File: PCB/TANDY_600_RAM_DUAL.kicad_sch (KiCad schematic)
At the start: 7 parts, among them CN1 TANDY_600_RAM_BUS, CN2 TANDY_600_RAM_BUS, U1 AS6C2008A, U2 74HC148, U3 74LVC1G02

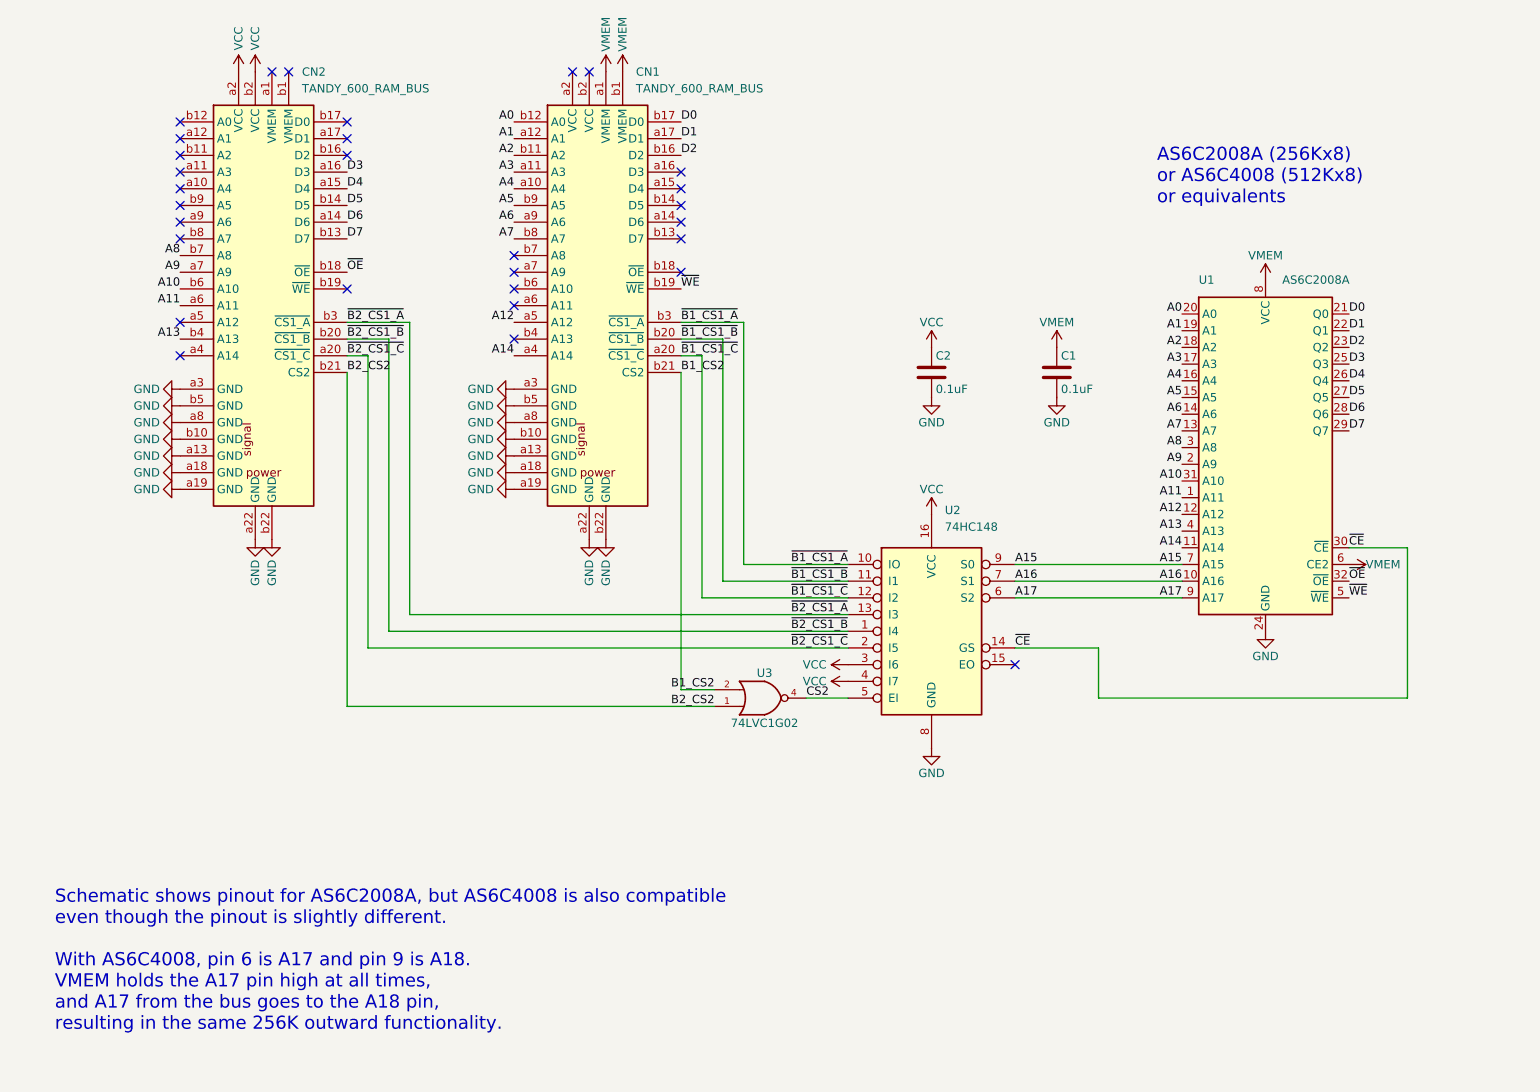
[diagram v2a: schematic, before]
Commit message: dual version add /CE pullup for battery life
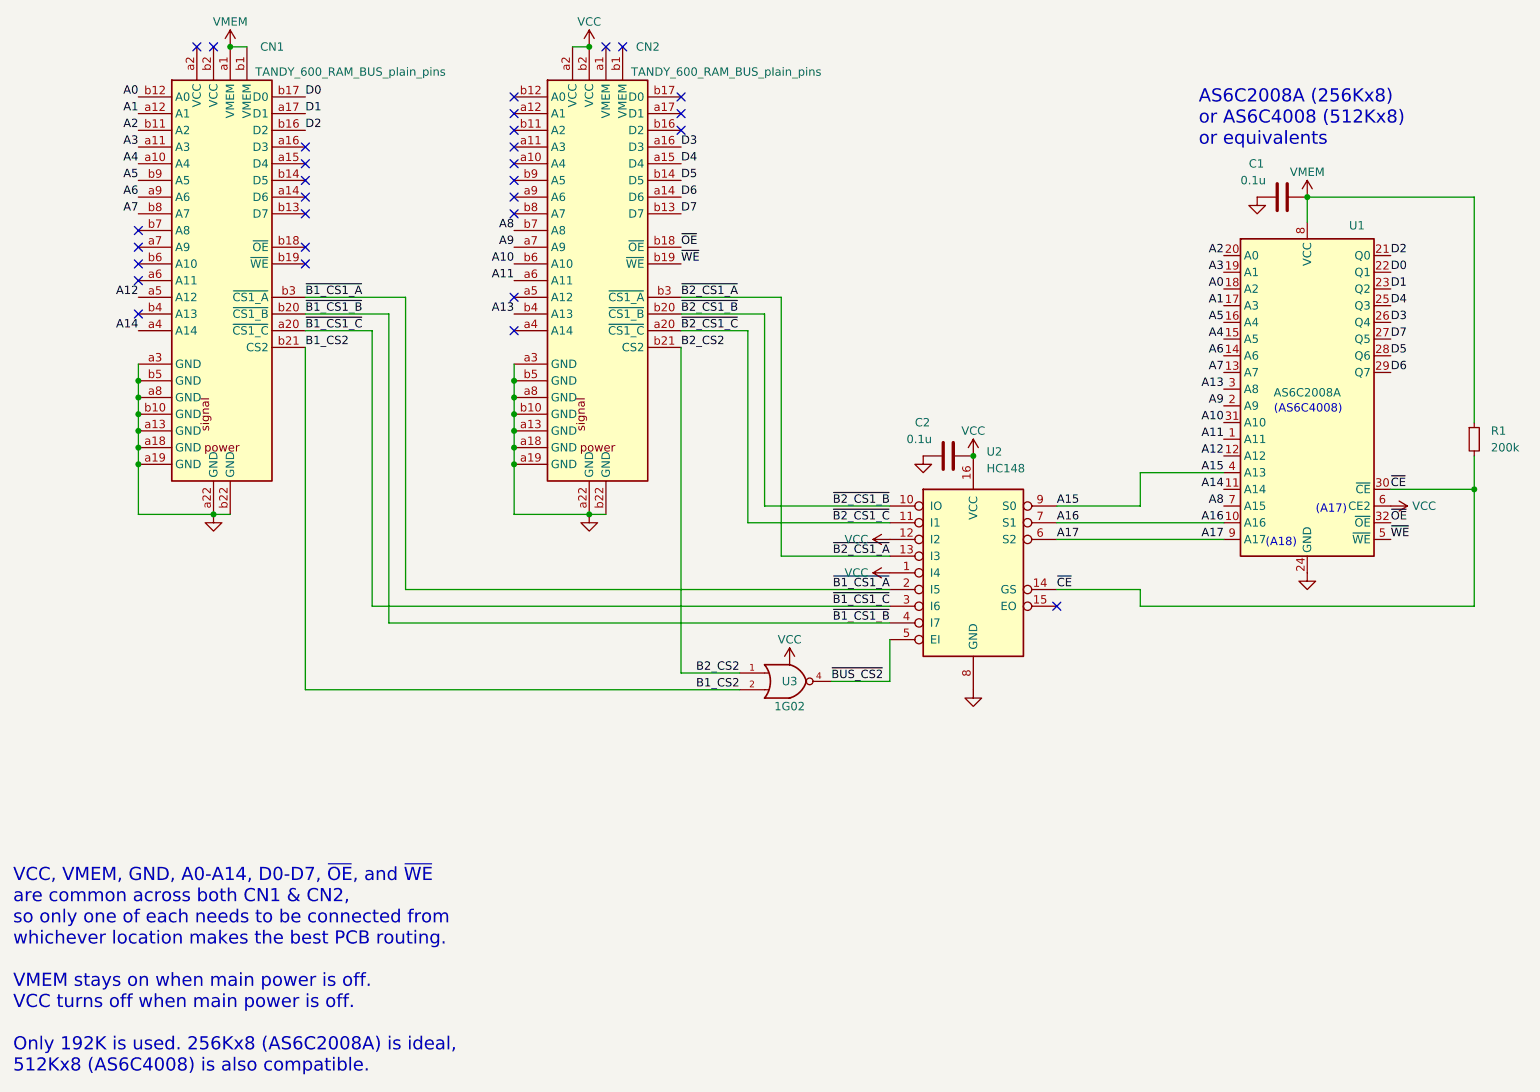
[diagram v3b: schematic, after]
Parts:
- added R1: 200k, 000_LOCAL:R_0805, symbol 000_LOCAL:R_Small
- C1, C2: value 0.1uF -> 0.1u
- CN1, CN2: value TANDY_600_RAM_BUS -> TANDY_600_RAM_BUS_plain_pins
- U2: value 74HC148 -> HC148
- U3: value 74LVC1G02 -> 1G02
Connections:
- net A0: now also U1.18 (A2); no longer U1.20 (A0)
- net A1: now also U1.17 (A3); no longer U1.19 (A1)
- net A13: now also U1.3 (A8); no longer U1.4 (A13)
- net A15: now also U1.4 (A13); no longer U1.7 (A15)
- net A2: now also U1.20 (A0); no longer U1.18 (A2)
- net A3: now also U1.19 (A1); no longer U1.17 (A3)
- net A4: now also U1.15 (A5); no longer U1.16 (A4)
- net A5: now also U1.16 (A4); no longer U1.15 (A5)
- net A8: now also U1.7 (A15); no longer U1.3 (A8)
- net D0: now also U1.22 (Q1); no longer U1.21 (Q0)
- net D1: now also U1.23 (Q2); no longer U1.22 (Q1)
- net D2: now also U1.21 (Q0); no longer U1.23 (Q2)
- net D3: now also U1.26 (Q4); no longer U1.25 (Q3)
- net D4: now also U1.25 (Q3); no longer U1.26 (Q4)
- net D5: now also U1.28 (Q6); no longer U1.27 (Q5)
- net D6: now also U1.29 (Q7); no longer U1.28 (Q6)
- net D7: now also U1.27 (Q5); no longer U1.29 (Q7)
- net VCC: now also U1.6 (CE2), U2.1 (I4), U2.12 (I2); no longer U2.3 (I6), U2.4 (I7)
- net VMEM: now also R1.1; no longer U1.6 (CE2)
- net ~{B1_CS1_A}: now also U2.2 (I5); no longer U2.10 (IO)
- net ~{B1_CS1_B}: now also U2.4 (I7); no longer U2.11 (I1)
- net ~{B1_CS1_C}: now also U2.3 (I6); no longer U2.12 (I2)
- net ~{B2_CS1_B}: now also U2.10 (IO); no longer U2.1 (I4)
- net ~{B2_CS1_C}: now also U2.11 (I1); no longer U2.2 (I5)
- net ~{CE}: now also R1.2
- net ~{WE}: now also CN2.b19 (~{WE}); no longer CN1.b19 (~{WE})
- net CS2 renamed ~{BUS_CS2}
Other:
- note added: "(A17)"
- note added: "(A18)"
- note added: "(AS6C4008)"
- note added: "VCC, VMEM, GND, A0-A14, D0-D7, ~{OE}, and ~{WE} are common across both CN1 & CN2, so only one of each needs to be connected from whichever location makes the best PCB routing. VMEM stays on when main power is off. VCC turns off when main power is off. Only 192K is used. 256Kx8 (AS6C2008A) is ideal, 512Kx8 (AS6C4008) is also compatible."
- note removed: "Schematic shows pinout for AS6C2008A, but AS6C4008 is also compatible even though the pinout is slightly different. With AS6C4008, pin 6 is A17 and pin 9 is A18. VMEM holds the A17 pin high at all times, and A17 from the bus goes to the A18 pin, resulting in the same 256K outward functionality."
- moved on the sheet: C1, C2, CN1, CN2, U1, U2, U3

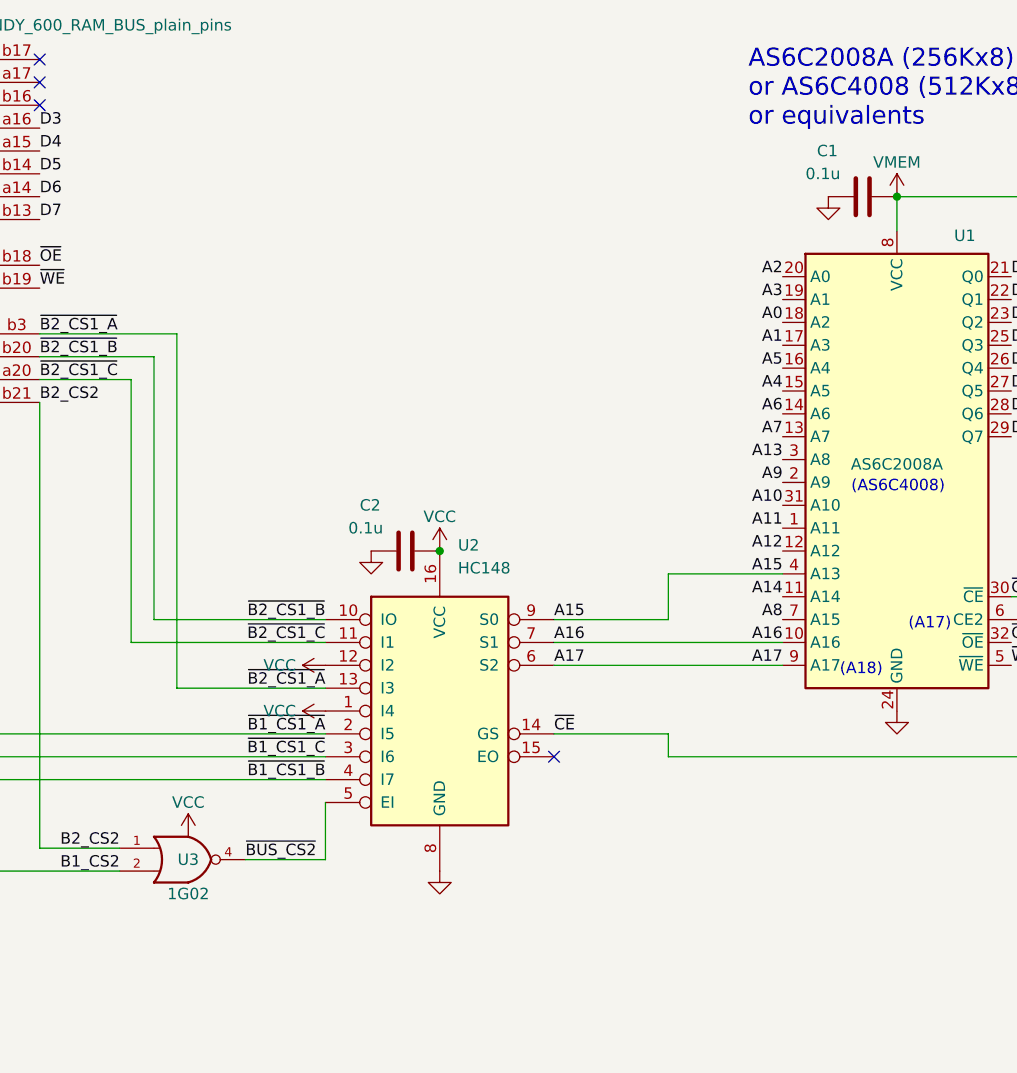
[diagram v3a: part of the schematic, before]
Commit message: footprints on dual
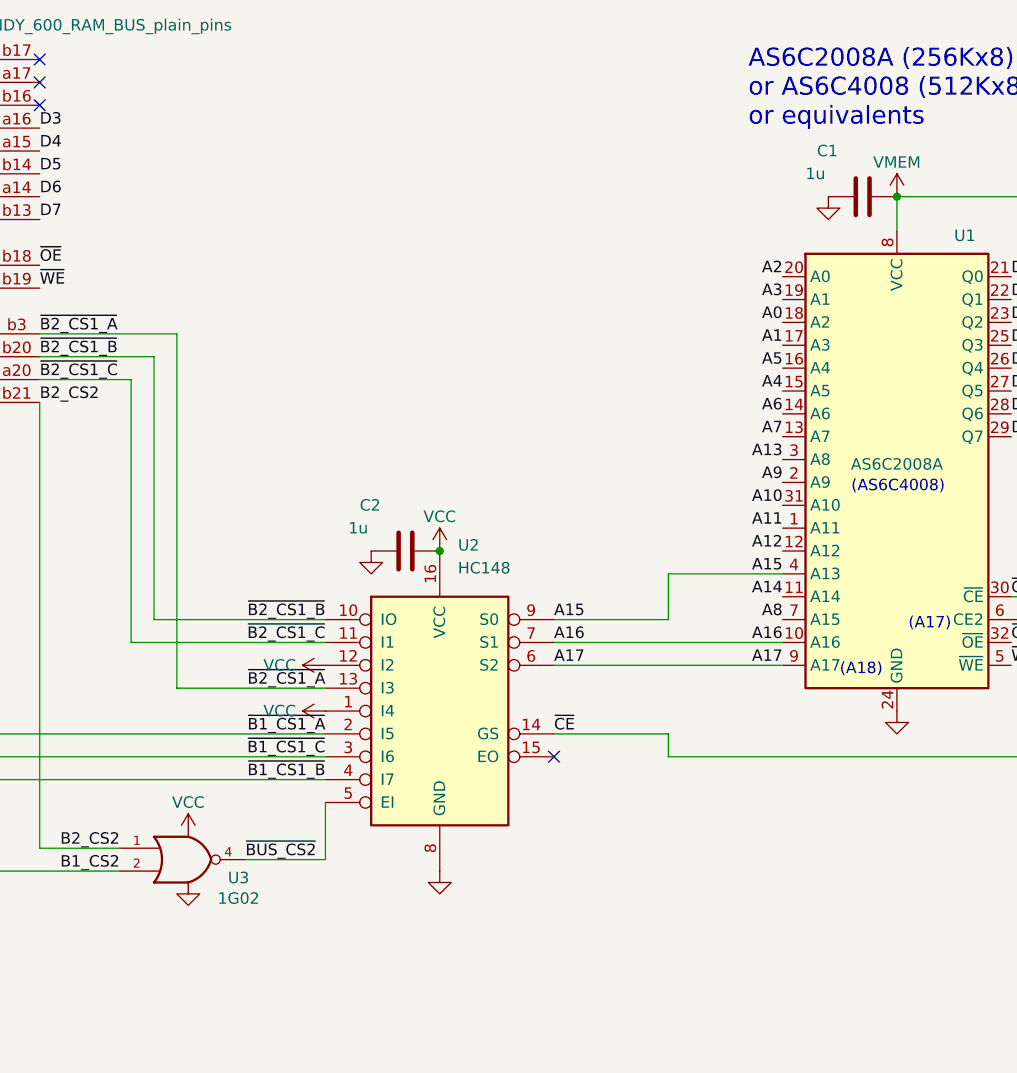
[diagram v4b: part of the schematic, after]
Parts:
- C1, C2: value 0.1u -> 1u

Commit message: rename 3d dir to 3dshapes to standardize
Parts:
- U2: footprint 000_LOCAL:SOIC-16_4x10 -> 000_LOCAL:SOIC-16_3.9x9.9mm_P1.27mm
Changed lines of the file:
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@@
 			)
 		)
-		(property "Footprint" "000_LOCAL:SOIC-16_4x10"
+		(property "Footprint" "000_LOCAL:SOIC-16_3.9x9.9mm_P1.27mm"
 			(at 165.1 120.65 0)
 			(effects

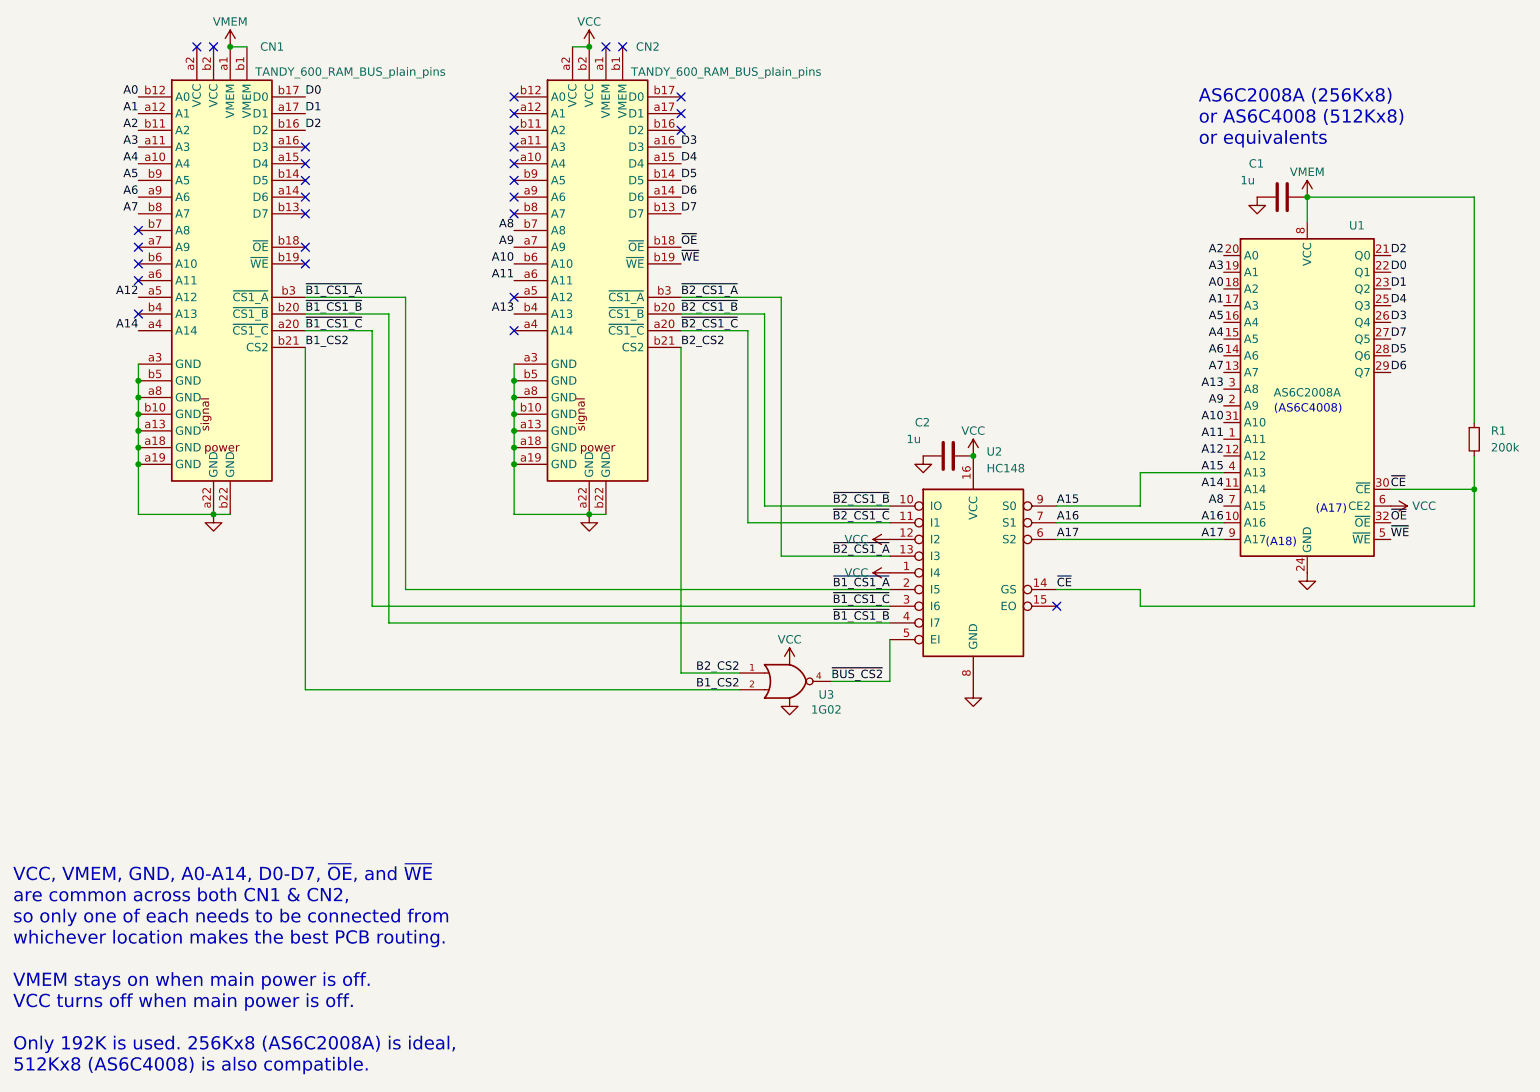
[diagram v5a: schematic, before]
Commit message: dual: sch add MPNs & bom, pcb move A14,16,17
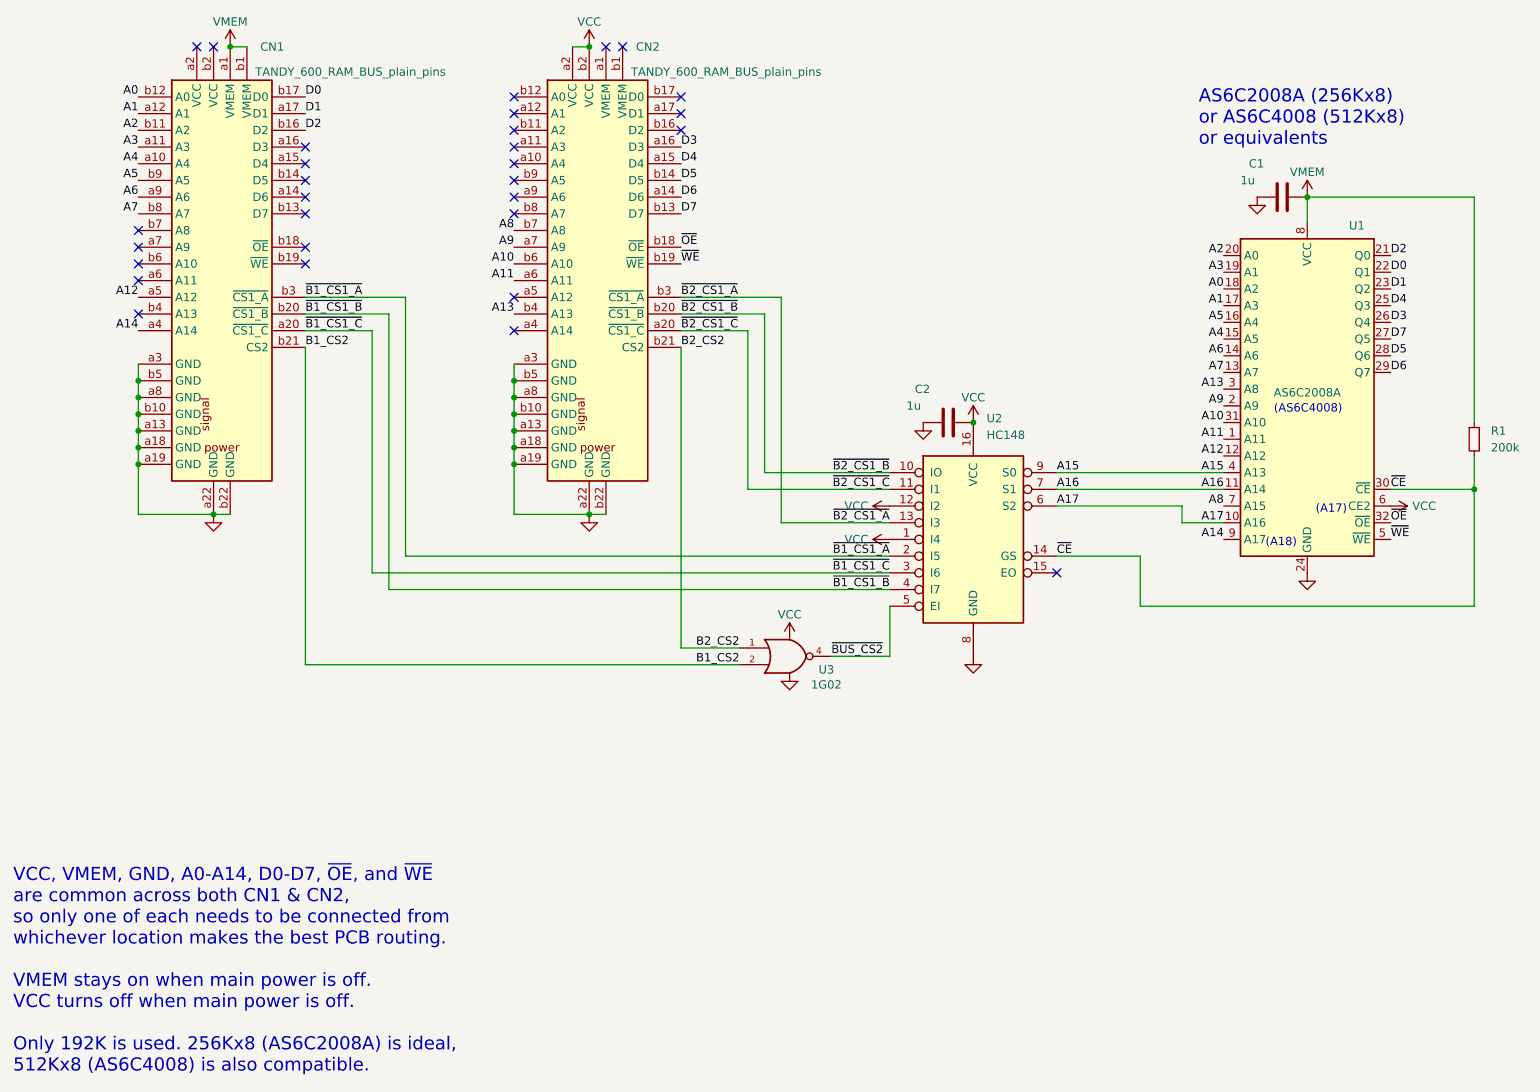
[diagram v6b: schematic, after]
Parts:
- C1, C2: MPN (none) -> CL21B105KAFNNNE
- CN1, CN2: MPN (none) -> PRPC022DAAN-RC
- R1: MPN (none) -> RMCF0805FT200K
- U1: MPN (none) -> AS6C4008-55STIN
- U2: MPN (none) -> SN74HC148DR
- U3: MPN (none) -> SN74AHC1G02DCKR
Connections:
- net A14: now also U1.9 (A17); no longer U1.11 (A14)
- net A16: now also U1.11 (A14); no longer U1.10 (A16)
- net A17: now also U1.10 (A16); no longer U1.9 (A17)
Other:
- moved on the sheet: C2, U2, U3
